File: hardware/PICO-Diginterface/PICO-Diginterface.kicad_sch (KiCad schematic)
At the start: 27 parts, among them U10 PC817C, U11 PC817C, U12 PC817C, U9 PC817C

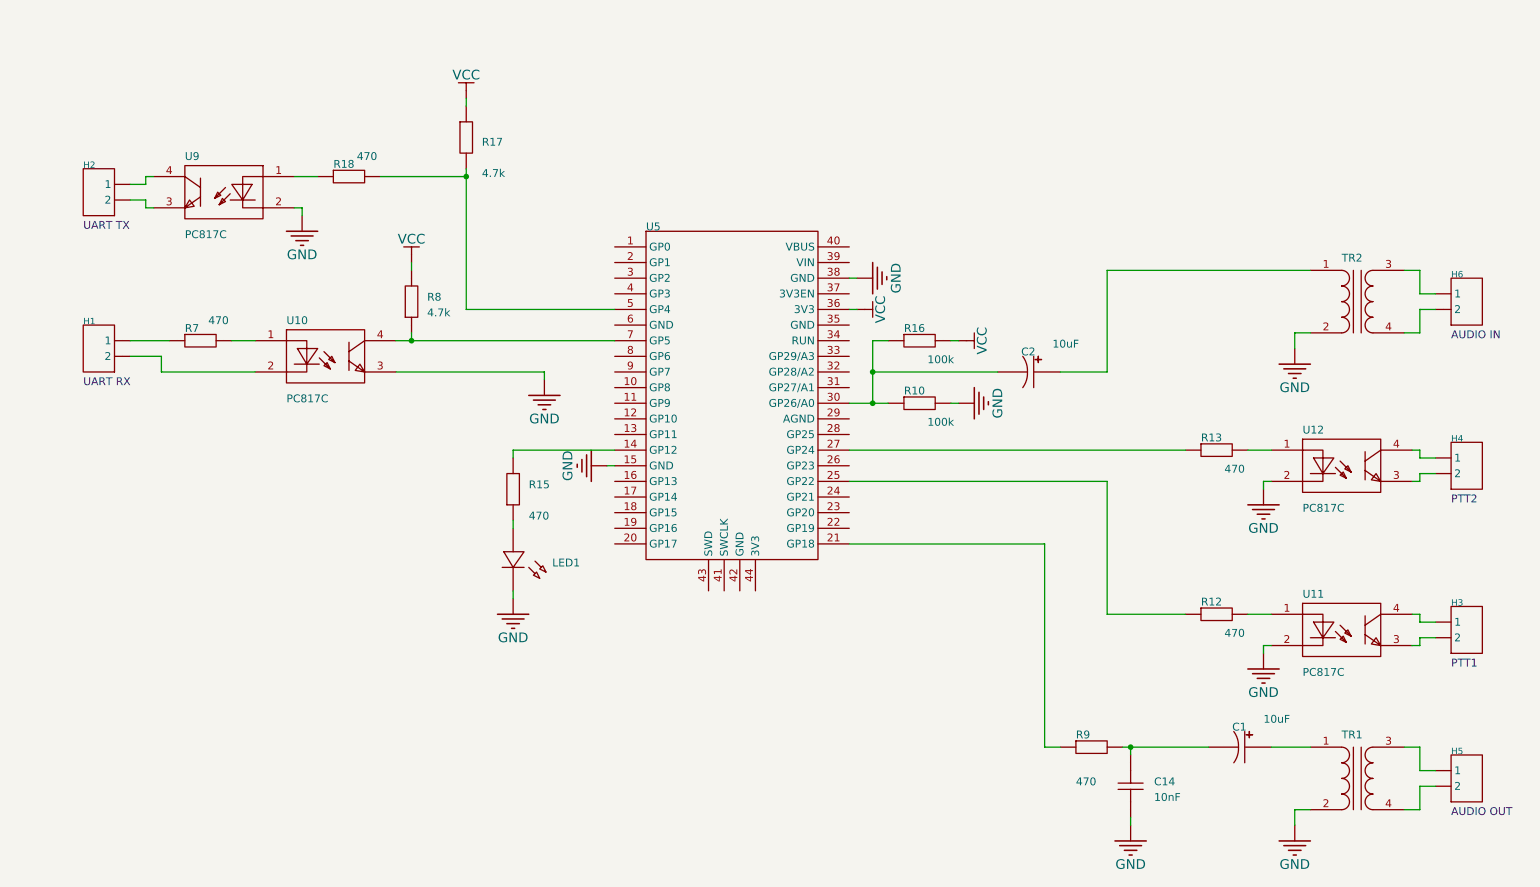
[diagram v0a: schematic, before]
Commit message: hardware change: common grounds on radio side
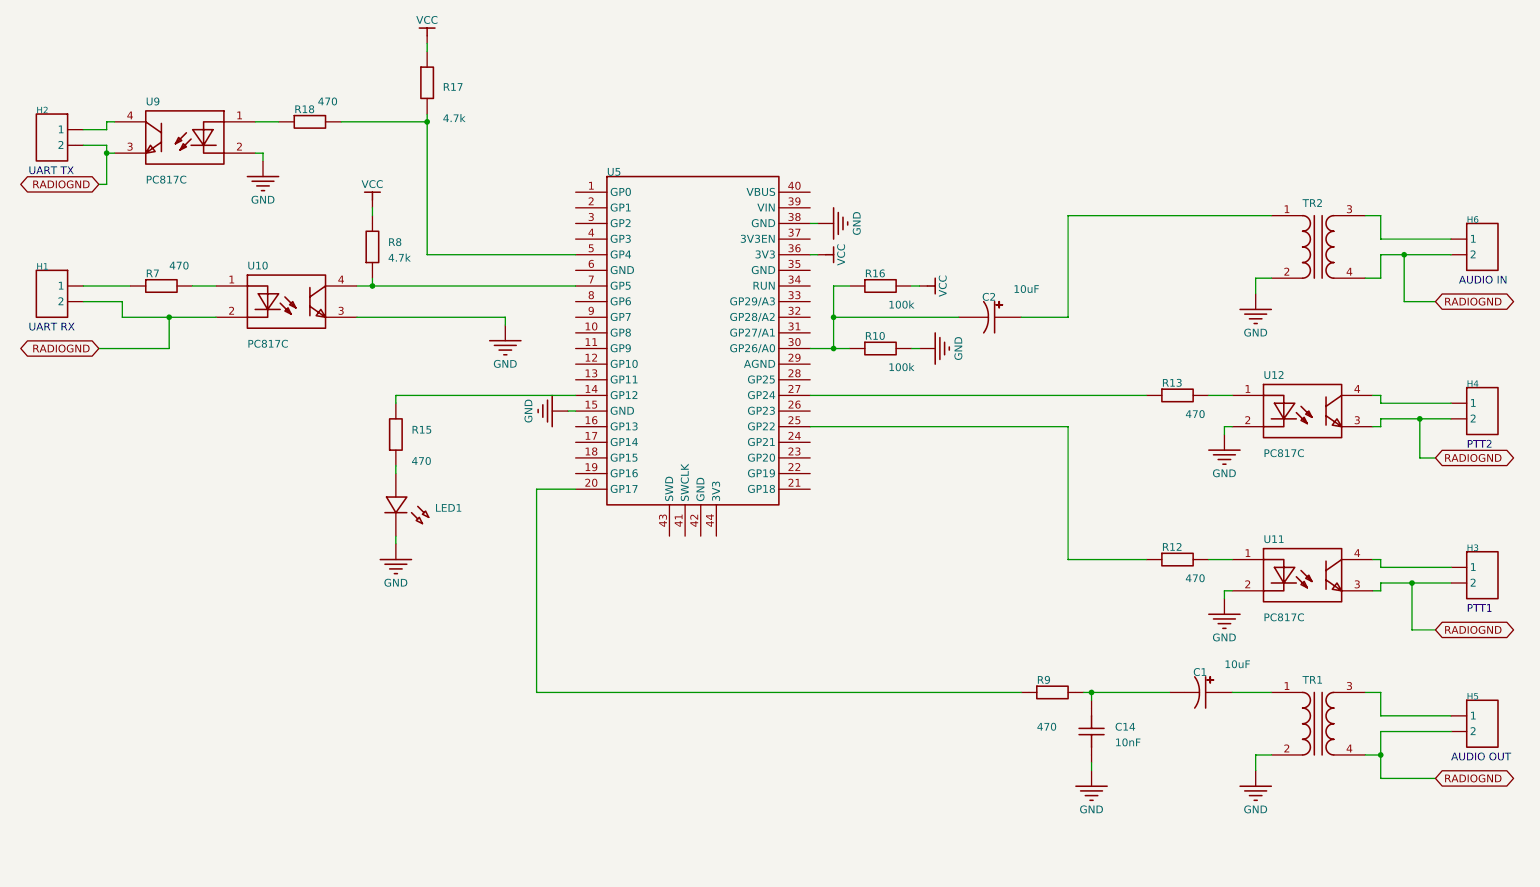
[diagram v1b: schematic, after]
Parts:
- removed C1, C2: 10uF, PICO-Digin-easyedapro:CAP-TH_BD12.5-P5.00-D0.6-FD, symbol PICO-Digin-easyedapro:ECR1EBK222MLL125025
- removed C14: 10nF, PICO-Digin-easyedapro:CAP-TH_L5.1-W3.2-P2.54-D0.5, symbol PICO-Digin-easyedapro:C322C103K5R5TA
- removed H1, H2, H3, H4, H5, H6: (no value), PICO-Digin-easyedapro:HDR-TH_2P-P2.54-V-F, symbol PICO-Digin-easyedapro:Header-Female-2.54_1x2
- removed LED1: (no value), PICO-Digin-easyedapro:LED-TH_BD3.0-P2.54-FD, symbol PICO-Digin-easyedapro:LED_TH-R
- removed R10, R16: 100k, PICO-Digin-easyedapro:R0603, symbol PICO-Digin-easyedapro:Res
- removed R12, R13, R15, R18, R7, R9: 470, PICO-Digin-easyedapro:R0603, symbol PICO-Digin-easyedapro:Res
- removed R17, R8: 4.7k, PICO-Digin-easyedapro:R0603, symbol PICO-Digin-easyedapro:Res
- removed TR1, TR2: TRANSFORMER AUDIO 1:1, PICO-Digin-easyedapro:, symbol PICO-Digin-easyedapro:TRANSFORMER AUDIO 1{colon}1
- removed U10, U11, U12, U9: PC817C, PICO-Digin-easyedapro:DIP-4_L4.6-W6.5-P2.54-LS7.6-BL, symbol PICO-Digin-easyedapro:PC817C_C20612449
- removed U5: (no value), PICO-Digin-easyedapro:PurplePICORP2040TH, symbol PICO-Digin-easyedapro:Purple-PICO-Rp2040
- added C1, C2: 10uF, ProPrj_PIC-easyedapro:CAP-TH_BD12.5-P5.00-D0.6-FD, symbol ProPrj_PIC-easyedapro:ECR1EBK222MLL125025
- added C14: 10nF, ProPrj_PIC-easyedapro:CAP-TH_L5.1-W3.2-P2.54-D0.5, symbol ProPrj_PIC-easyedapro:C322C103K5R5TA
- added H1, H2, H3, H4, H5, H6: (no value), ProPrj_PIC-easyedapro:HDR-TH_2P-P2.54-V-F, symbol ProPrj_PIC-easyedapro:Header-Female-2.54_1x2
- added LED1: (no value), ProPrj_PIC-easyedapro:LED-TH_BD3.0-P2.54-FD, symbol ProPrj_PIC-easyedapro:LED_TH-R
- added R10, R16: 100k, ProPrj_PIC-easyedapro:R0603, symbol ProPrj_PIC-easyedapro:Res
- added R12, R13, R15, R18, R7, R9: 470, ProPrj_PIC-easyedapro:R0603, symbol ProPrj_PIC-easyedapro:Res
- added R17, R8: 4.7k, ProPrj_PIC-easyedapro:R0603, symbol ProPrj_PIC-easyedapro:Res
- added TR1, TR2: TRANSFORMER AUDIO 1:1, ProPrj_PIC-easyedapro:, symbol ProPrj_PIC-easyedapro:TRANSFORMER AUDIO 1{colon}1
- added U10, U11, U12, U9: PC817C, ProPrj_PIC-easyedapro:DIP-4_L4.6-W6.5-P2.54-LS7.6-BL, symbol ProPrj_PIC-easyedapro:PC817C_C20612449
- added U5: (no value), ProPrj_PIC-easyedapro:PurplePICORP2040TH, symbol ProPrj_PIC-easyedapro:Purple-PICO-Rp2040
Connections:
- net GND: now also C14.1, LED1.2 (A), R10.2, TR1.2, TR2.2, U10.3 (EM), U11.2 (CAT), U12.2 (CAT), U5.15 (GND), U5.38 (GND), U9.2 (CAT)
- net VCC: now also R16.2, R17.1, R8.2, U5.36 (3V3)
- new net: H1.1, R7.1
- new net: R7.2, U10.1 (AN)
- new net: C2.1, TR2.1
- new net: H6.1, TR2.3
- new net: C1.1, TR1.1
- new net: C1.2, C14.2, R9.2
- new net: C2.2, R10.1, R16.1, U5.30 (GP26/A0)
- new net: R12.2, U11.1 (AN)
- new net: H3.1, U11.4 (COL)
- new net: R13.1, U5.27 (GP24)
- new net: R13.2, U12.1 (AN)
- new net: R12.1, U5.25 (GP22)
- new net: H5.1, TR1.3
- new net: LED1.1 (C), R15.1
- new net: R15.2, U5.14 (GP12)
- new net: R17.2, R18.2, U5.5 (GP4)
- new net: R8.1, U10.4 (COL), U5.7 (GP5)
- new net: H4.1, U12.4 (COL)
- new net: R9.1, U5.20 (GP17)
- new net: H2.1, U9.4 (COL)
- new net: R18.1, U9.1 (AN)
- new net RADIOGND: H1.2, H2.2, H3.2, H4.2, H5.2, H6.2, TR1.4, TR2.4, U10.2 (CAT), U11.3 (EM), U12.3 (EM), U9.3 (EM)
